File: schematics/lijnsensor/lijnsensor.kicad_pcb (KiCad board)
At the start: 2 copper layers, 137 x 105 mm, 29 parts, among them J1 Conn_01x04_Pin, U10 AS7343xDLG, U11 AS7343xDLG, U2 TCA9548APWR, U3 TLV75718PDBV, U4 AS7343xDLG, U5 AS7343xDLG, U6 AS7343xDLG, U7 AS7343xDLG, U8 AS7343xDLG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

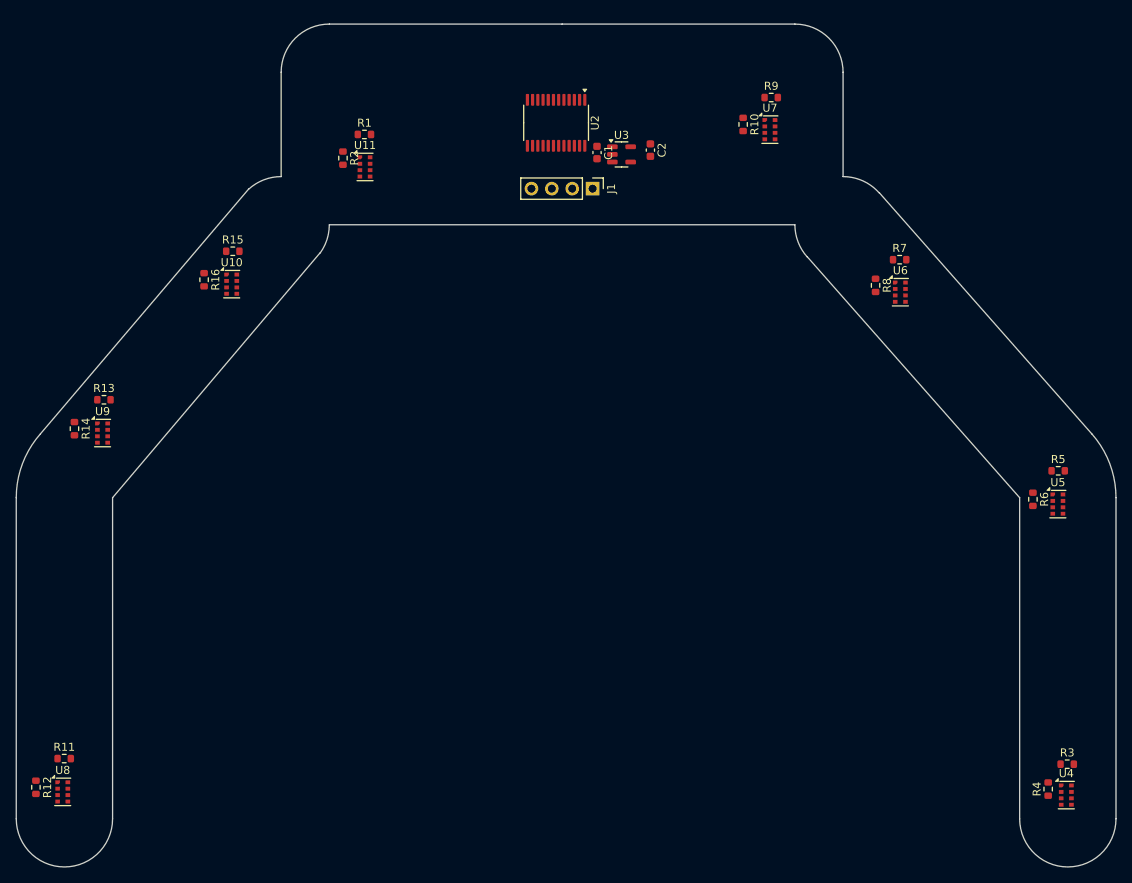
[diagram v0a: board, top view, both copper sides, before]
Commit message: ESD bescherming voor de lijnsensor
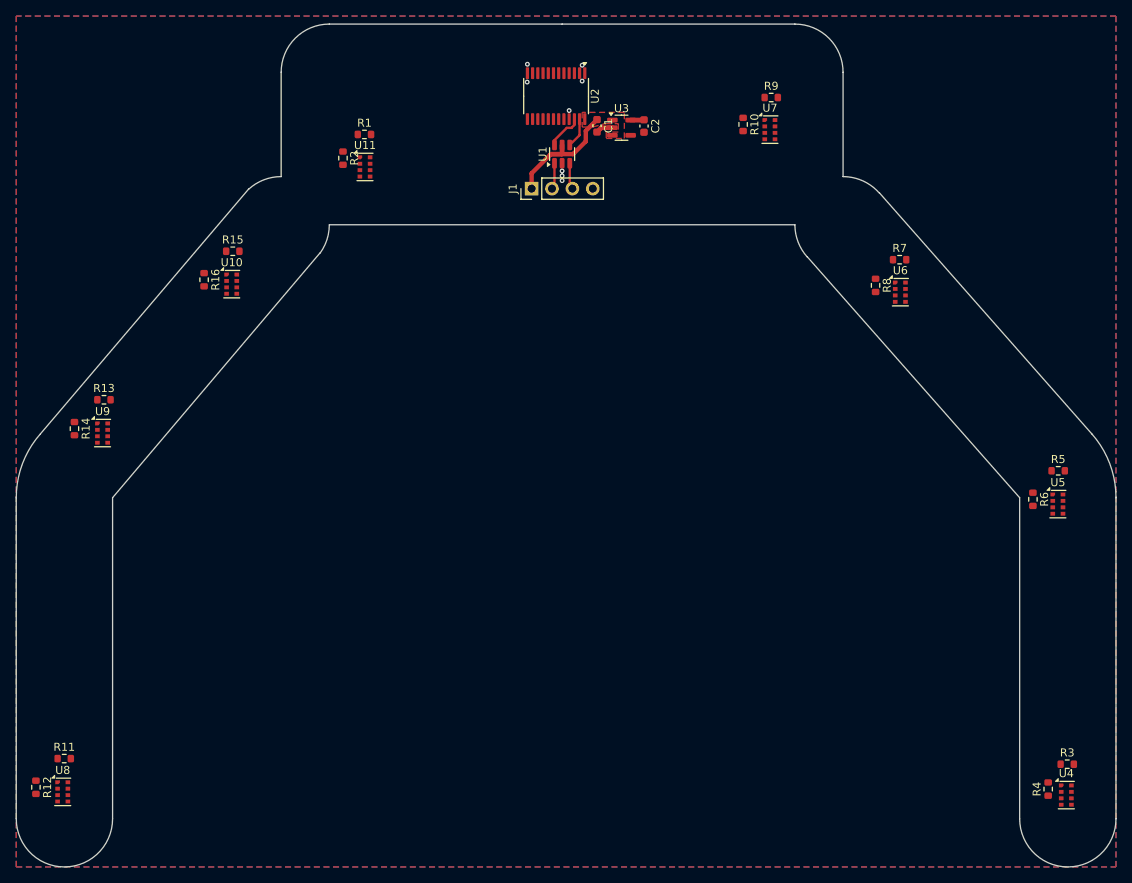
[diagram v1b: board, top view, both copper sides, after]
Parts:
- added U1: USBLC6-2SC6, Package_TO_SOT_SMD:SOT-23-6, F.Cu at (118.0, 67.2)
- moved J1 7.60 mm to (114.2, 71.5), turned to 90 degrees
- moved U3 3.33 mm to (125.4, 63.9)
- moved C1 3.33 mm to (122.3, 63.7)
- moved U2 3.32 mm to (117.2, 60.0)
- moved C2 3.10 mm to (128.2, 63.7)
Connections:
- J1 pad 2: /SDA -> Net-(J1-Pin_2)
- J1 pad 3: /SCL -> Net-(J1-Pin_3)
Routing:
- net +3.3V: track 0.00 -> 16.1 mm
- net /SCL: track 0.00 -> 4.59 mm
- net Net-(J1-Pin_2): track 0.00 -> 3.76 mm
- net /SDA: track 0.00 -> 3.73 mm
- net Net-(J1-Pin_3): track 0.00 -> 3.30 mm
- net GND: track 0.00 -> 2.14 mm, vias 0 -> 8
- net +1V8: track 0.00 -> 1.68 mm
- added copper zone on F.Cu, net +3.3V
- added copper zone on B.Cu, net GND
- added copper zone on F.Cu, net GND

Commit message: de routing is klaar van de lijnsensor nog allen opschonen
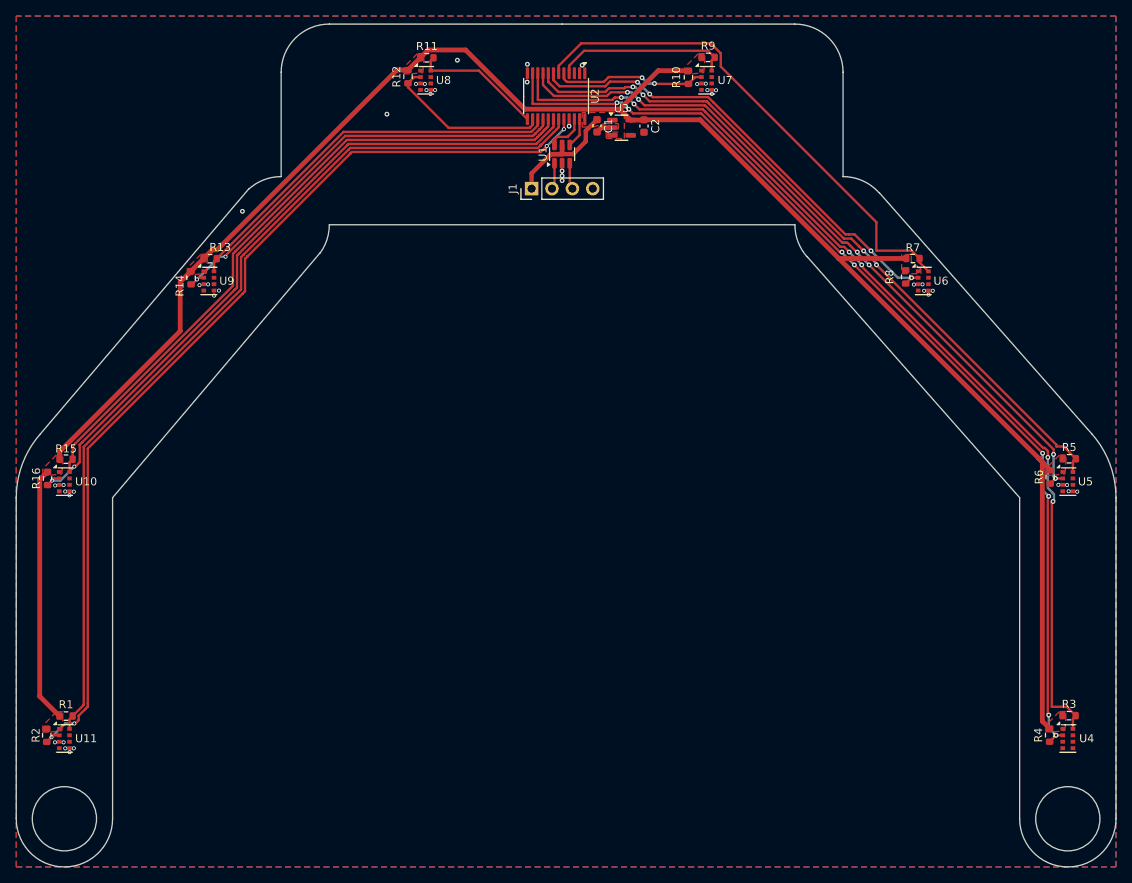
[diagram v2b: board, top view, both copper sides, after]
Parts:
- moved R12 99.9 mm to (98.8, 57.5)
- moved U8 99.5 mm to (101.0, 58.0)
- moved R11 98.3 mm to (101.2, 55.2)
- moved R1 81.4 mm to (56.2, 137.2)
- moved R2 80.8 mm to (53.8, 139.6)
- moved U11 80.4 mm to (56.0, 140.0)
- moved R15 33.2 mm to (56.2, 105.2)
- moved U10 32.2 mm to (56.0, 108.0)
- moved R16 31.5 mm to (53.9, 107.6)
- moved R14 23.8 mm to (71.8, 82.6)
- moved U9 23.1 mm to (74.0, 83.0)
- moved R13 22.0 mm to (74.2, 80.2)
- moved U7 10.0 mm to (136.0, 58.0)
- moved R9 9.32 mm to (136.2, 55.1)
- moved R10 9.00 mm to (133.7, 57.6)
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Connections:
- R10 pad 2: Net-(U2-SC3) -> Net-(U2-SC0)
- R3 pad 2: Net-(U2-SD0) -> Net-(U2-SD3)
- R4 pad 2: Net-(U2-SC0) -> Net-(U2-SC3)
- R5 pad 2: Net-(U2-SD1) -> Net-(U2-SD2)
- R6 pad 2: Net-(U2-SC1) -> Net-(U2-SC2)
- R7 pad 2: Net-(U2-SD2) -> Net-(U2-SD1)
- R8 pad 2: Net-(U2-SC2) -> Net-(U2-SC1)
- R9 pad 2: Net-(U2-SD3) -> Net-(U2-SD0)
- U4 pad 2: Net-(U2-SC0) -> Net-(U2-SC3)
- U4 pad 8: Net-(U2-SD0) -> Net-(U2-SD3)
- U5 pad 2: Net-(U2-SC1) -> Net-(U2-SC2)
- U5 pad 8: Net-(U2-SD1) -> Net-(U2-SD2)
- U6 pad 2: Net-(U2-SC2) -> Net-(U2-SC1)
- U6 pad 8: Net-(U2-SD2) -> Net-(U2-SD1)
- U7 pad 2: Net-(U2-SC3) -> Net-(U2-SC0)
- U7 pad 8: Net-(U2-SD3) -> Net-(U2-SD0)
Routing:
- net +1V8: track 1.68 -> 255.5 mm
- net Net-(U2-SC3): track 0.00 -> 123.4 mm, vias 0 -> 8
- net Net-(U2-SD3): track 0.00 -> 122.9 mm, vias 0 -> 6
- net Net-(U11-SCL): track 0.00 -> 119.9 mm, vias 0 -> 4
- net Net-(U11-SDA): track 0.00 -> 115.1 mm
- net Net-(U2-SC2): track 0.00 -> 90.3 mm, vias 0 -> 6
- net Net-(U2-SD2): track 0.00 -> 88.9 mm, vias 0 -> 4
- net Net-(U10-SCL): track 0.00 -> 87.1 mm, vias 0 -> 2
- net Net-(U10-SDA): track 0.00 -> 82.4 mm
- net Net-(U2-SD1): track 0.00 -> 63.2 mm
- net Net-(U2-SC1): track 0.00 -> 58.0 mm, vias 0 -> 4
- net Net-(U2-SC5): track 0.00 -> 53.8 mm, vias 0 -> 2
- net Net-(U2-SD5): track 0.00 -> 49.4 mm
- net Net-(U2-SD0): track 0.00 -> 22.0 mm
- net Net-(U2-SC4): track 0.00 -> 20.9 mm
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- added copper zone on F.Cu, net +1V8
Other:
- outline, holes or cut-outs redrawn

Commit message: lijnsensor is klaar
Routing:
- net Net-(U2-SC3): track 123.4 -> 122.0 mm
- net Net-(U2-SD3): track 122.9 -> 121.7 mm
- net GND: vias 43 -> 49
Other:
- outline, holes or cut-outs redrawn

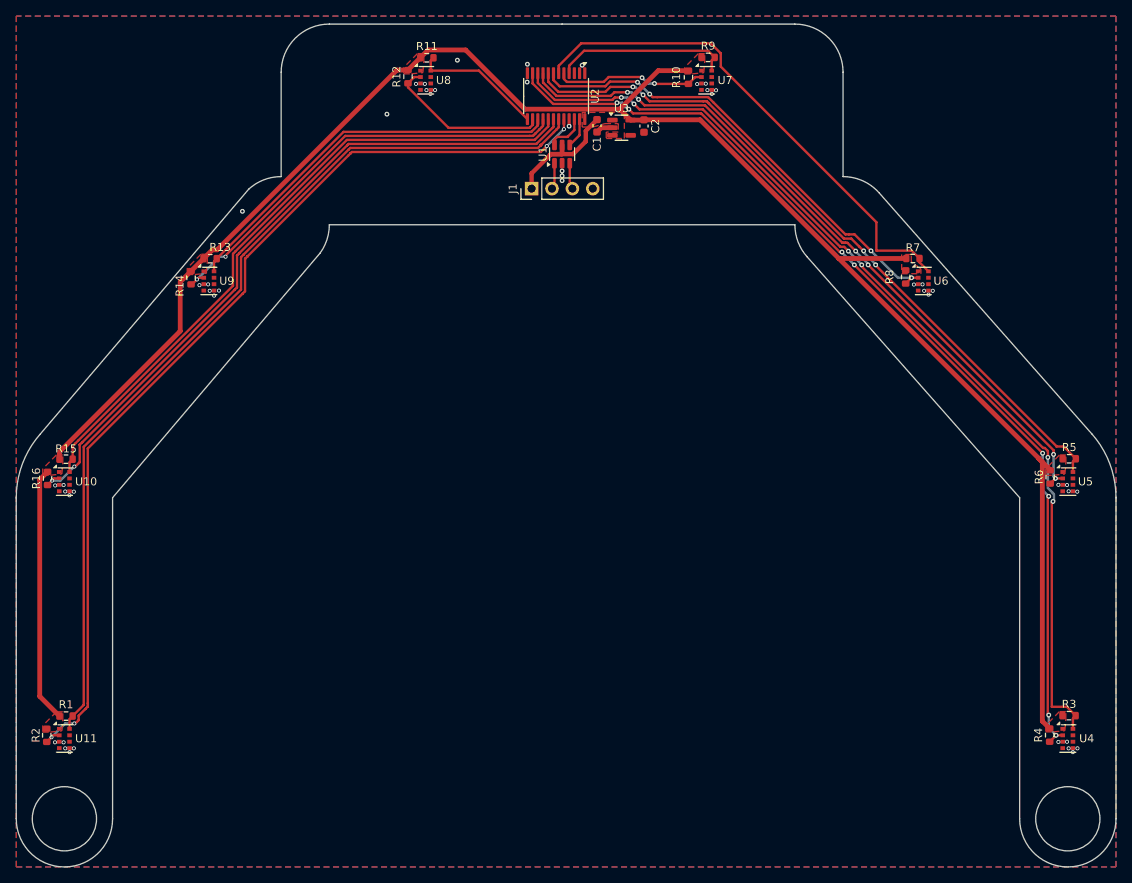
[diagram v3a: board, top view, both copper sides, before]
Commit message: voeg de gaten toe om te kunnen vastvijzen
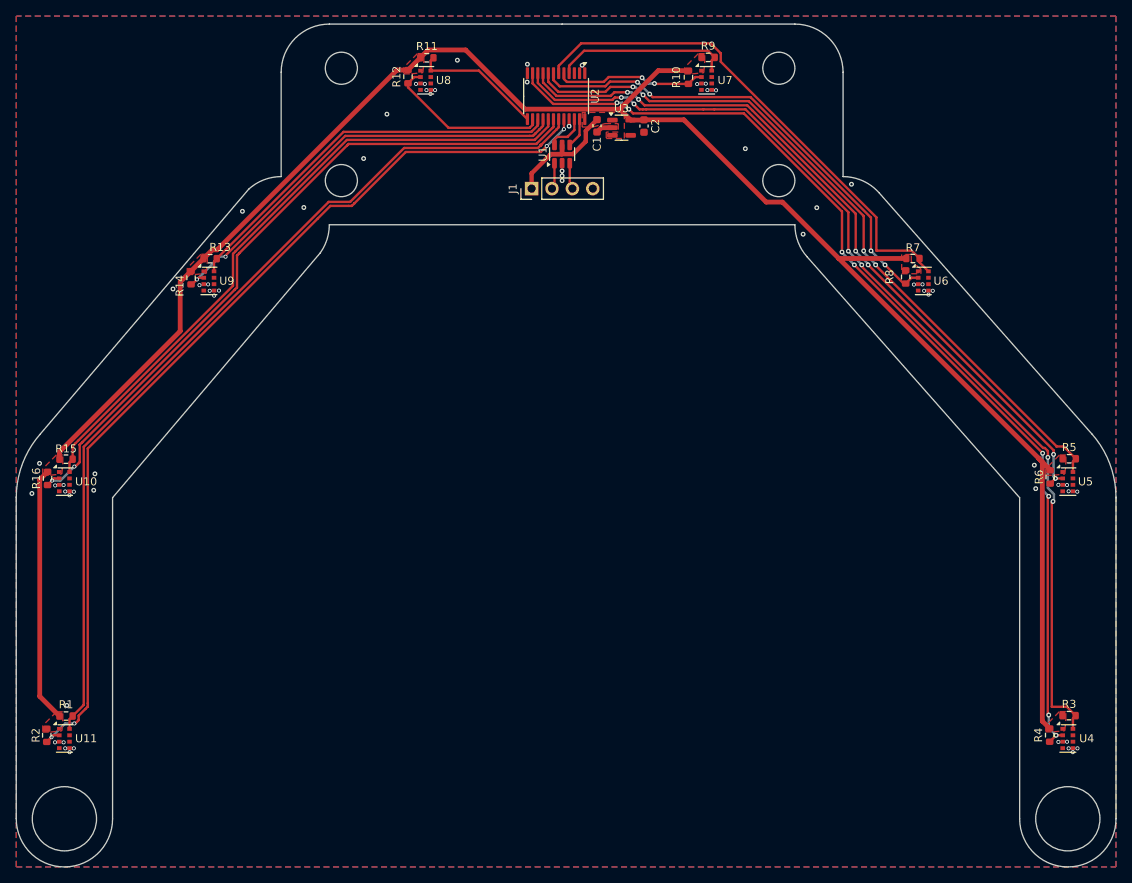
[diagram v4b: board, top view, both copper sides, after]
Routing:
- net Net-(U2-SC3): track 122.0 -> 124.9 mm
- net Net-(U2-SD3): track 121.7 -> 124.5 mm
- net Net-(U2-SD2): track 89.0 -> 91.5 mm
- net Net-(U11-SCL): track 119.9 -> 117.5 mm
- net Net-(U11-SDA): track 115.1 -> 112.7 mm
- net Net-(U2-SC2): track 90.1 -> 92.4 mm
- net Net-(U2-SC1): track 58.0 -> 60.0 mm
- net GND: vias 49 -> 62
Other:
- outline, holes or cut-outs redrawn
